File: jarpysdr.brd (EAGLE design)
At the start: 90 x 45 mm, 40 parts

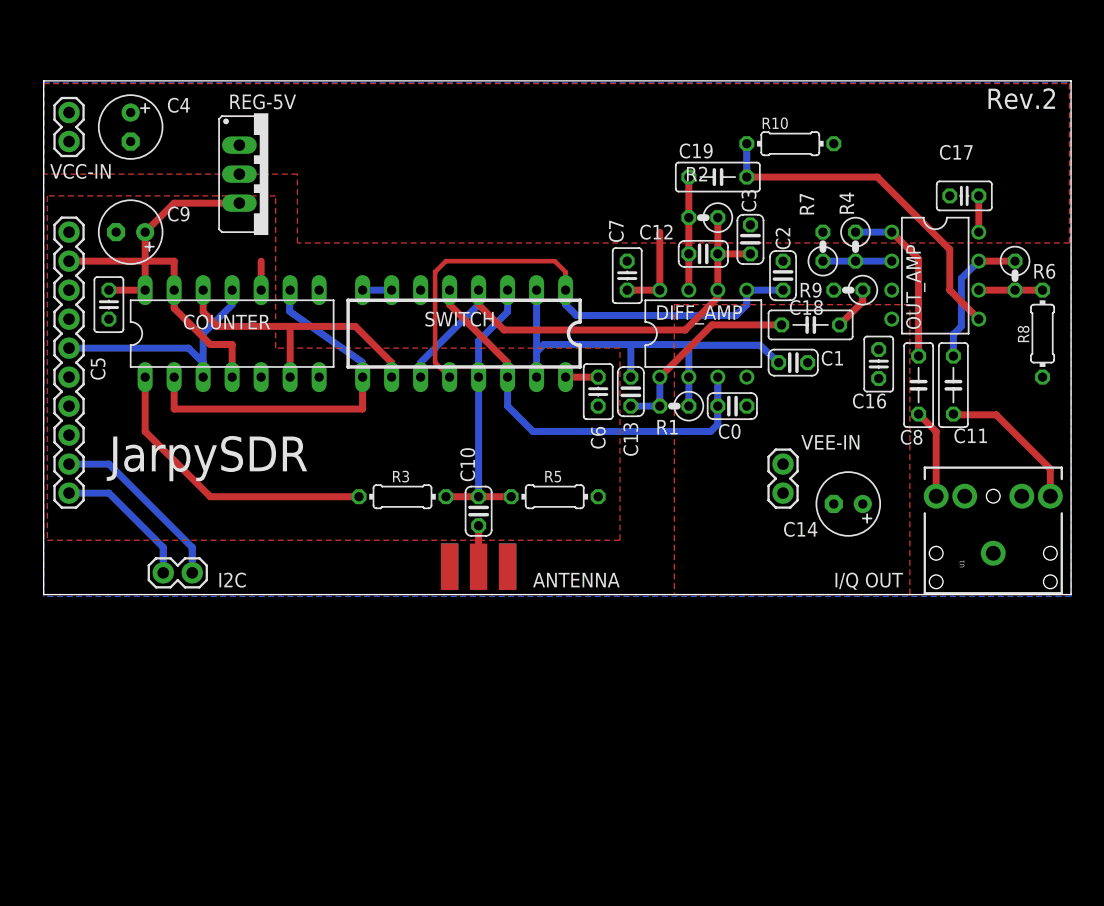
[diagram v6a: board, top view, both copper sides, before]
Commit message: New layout. 50x50mm board.
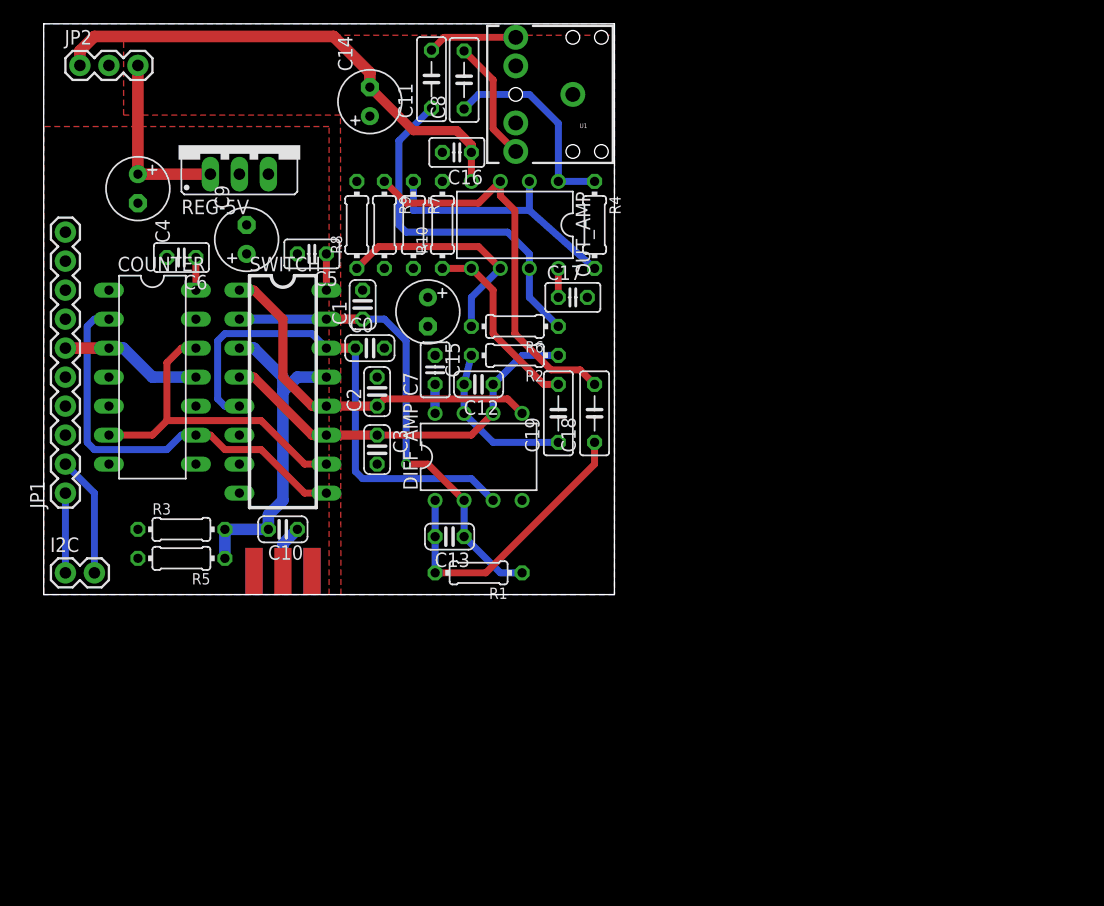
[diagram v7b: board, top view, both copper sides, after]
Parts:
- removed VCC-IN: +12V, SparkFun:1X02
- removed VEE-IN: -12v, SparkFun:1X02
- added C15: 10u, resistor:E2,5-6
- added JP2: JUMPER-3PTH, SparkFun:1X03
- R1, R2, R4, R6, R7, R9: device resistor:0207/2V -> resistor:0204/7
- moved R8 60.8 mm to (27.4, 32.4), turned to 90 degrees
- moved C14 54.8 mm to (28.6, 43.2), turned to 90 degrees
- moved U1 54.5 mm to (46.4, 43.8), turned to 180 degrees
- moved C11 53.0 mm to (34.0, 45.1), turned to 90 degrees
- moved C8 48.0 mm to (36.8, 45.1), turned to 90 degrees
- moved R6 44.0 mm to (41.3, 23.5), turned to 180 degrees
- moved C16 41.3 mm to (36.2, 38.7), turned to 180 degrees
- moved R9 41.0 mm to (29.8, 32.4), turned to 270 degrees
- moved C6 38.4 mm to (12.1, 29.5), turned to 180 degrees
- moved C1 38.1 mm to (27.9, 25.4), turned to 90 degrees
- moved C3 37.5 mm to (29.2, 12.7), turned to 270 degrees
- moved OUT_AMP 37.1 mm to (41.3, 32.4), turned to 180 degrees
- moved C2 37.0 mm to (29.2, 17.8)
- moved R7 35.9 mm to (32.4, 32.4), turned to 270 degrees
- moved C17 35.4 mm to (46.4, 26.0), turned to 0 degrees
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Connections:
- net +12V: now also C15.+, JP2.3; no longer VCC-IN.2
- net -12V: now also JP2.1; no longer VEE-IN.1
- net GND: now also C15.-, JP2.2; no longer VCC-IN.1, VEE-IN.2
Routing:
- net +5V: track 71.4 -> 6.03 mm
- net -12V: track 0.00 -> 44.0 mm
- net N$18: track 3.89 -> 34.4 mm
- net N$13: track 12.4 -> 31.3 mm
- net N$12: track 6.03 -> 22.9 mm
- net N$15: track 5.59 -> 20.3 mm
- net N$19: track 30.5 -> 16.6 mm
- net N$1: track 45.9 -> 32.7 mm
- net +12V: track 11.1 -> 21.0 mm
- net CLK: track 22.2 -> 12.5 mm
- net N$14: track 43.9 -> 34.4 mm
- net N$6: track 17.6 -> 26.2 mm
- net N$5: track 36.0 -> 44.0 mm
- net N$16: track 12.5 -> 6.99 mm
- net N$17: track 16.0 -> 10.6 mm
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- removed copper zone on layer 1, net -12V
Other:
- board size 90 x 45 mm -> 50 x 50 mm
- board text removed: "ANTENNA"
- board text removed: "I/Q OUT"
- board text removed: "JarpySDR"
- board text removed: "Rev.2"
